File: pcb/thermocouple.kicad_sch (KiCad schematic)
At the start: 3 parts, among them J2 Conn_01x02, U4 MCP96RL00T-E_MX

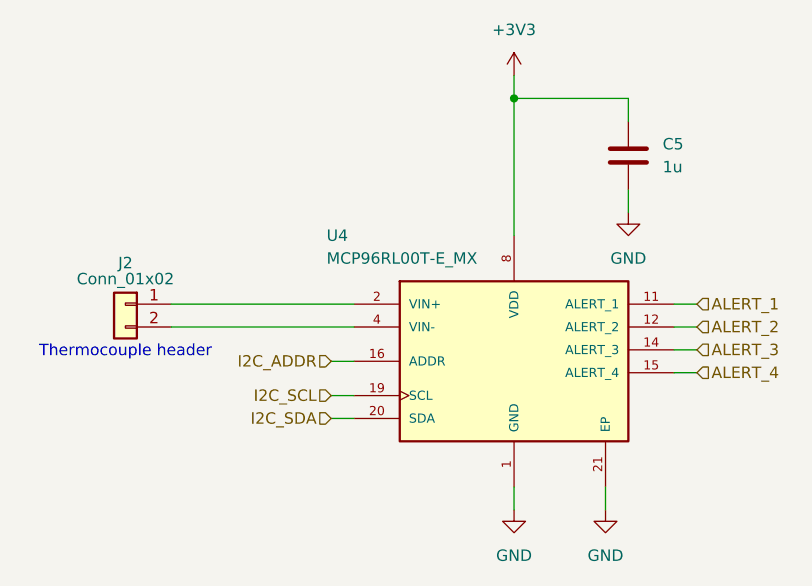
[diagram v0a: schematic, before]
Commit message: Update schematic for DE15
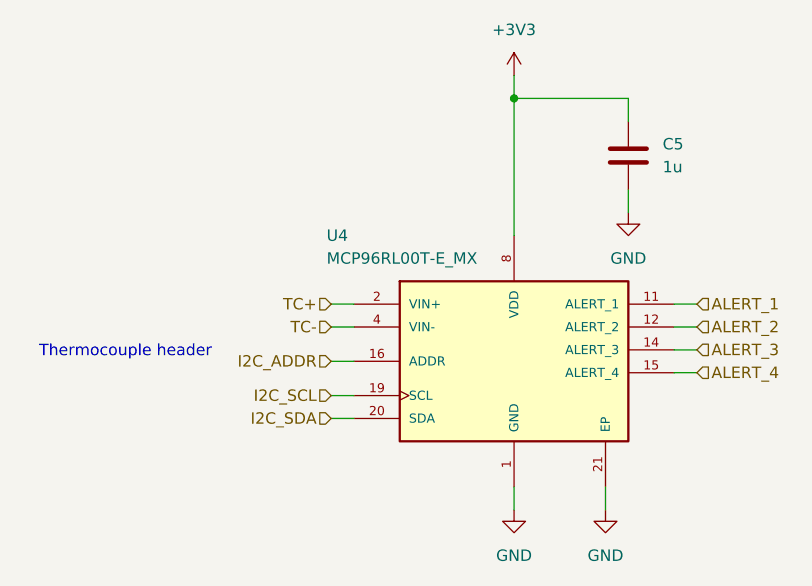
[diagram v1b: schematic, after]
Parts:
- removed J2: Conn_01x02, Connector_PinHeader_2.54mm:PinHeader_1x02_P2.54mm_Vertical, symbol Connector_Generic:Conn_01x02
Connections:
- net TC+: now reaches U4.2 (VIN+)
- net TC-: now reaches U4.4 (VIN-)
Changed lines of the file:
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@@
+	(wire
+		(pts
+			(xy 119.38 76.2) (xy 121.92 76.2)
+		)
+		(stroke
+			(width 0)
+			(type default)
+		)
+	)
+	(wire
+		(pts
+			(xy 119.38 78.74) (xy 121.92 78.74)
+		)
+		(stroke
+			(width 0)
+			(type default)
+		)
+	)
 	(wire
 		(pts
@@
 	(wire
 		(pts
-			(xy 101.6 78.74) (xy 121.92 78.74)
-		)
-		(stroke
-			(width 0)
-			(type default)
-		)
-	)
-	(wire
-		(pts
-			(xy 101.6 76.2) (xy 121.92 76.2)
-		)
-		(stroke
-			(width 0)
-			(type default)
-		)
-	)
-	(wire
-		(pts
 			(xy 119.38 86.36) (xy 121.92 86.36)
 		)
@@
 		)
 	)
+	(hierarchical_label "TC-"
+		(shape input)
+		(at 119.38 78.74 180)
+		(effects
+			(font
+				(size 1.27 1.27)
+			)
+			(justify right)
+		)
+	)
 	(hierarchical_label "ALERT_1"
 		(shape input)
@@
 			)
 			(justify left)
+		)
+	)
+	(hierarchical_label "TC+"
+		(shape input)
+		(at 119.38 76.2 180)
+		(effects
+			(font
+				(size 1.27 1.27)
+			)
+			(justify right)
 		)
 	)
@@
 					(unit 1)
 				)
-			)
-		)
-	)
-	(symbol
-		(lib_id "Connector_Generic:Conn_01x02")
-		(at 96.52 76.2 0)
-		(mirror y)
-		(unit 1)
-		(exclude_from_sim no)
-		(in_bom yes)
-		(on_board yes)
-		(dnp no)
-		(property "Reference" "J2"
-			(at 96.52 71.628 0)
-			(effects
-				(font
-					(size 1.27 1.27)
-				)
-			)
-		)
-		(property "Value" "Conn_01x02"
-			(at 96.52 73.406 0)
-			(effects
-				(font
-					(size 1.27 1.27)
-				)
-			)
-		)
-		(property "Footprint" "Connector_PinHeader_2.54mm:PinHeader_1x02_P2.54mm_Vertical"
-			(at 96.52 76.2 0)
-			(effects
-				(font
-					(size 1.27 1.27)
-				)
-				(hide yes)
-			)
-		)
-		(property "Datasheet" "~"
-			(at 96.52 76.2 0)
-			(effects
-				(font
-					(size 1.27 1.27)
-				)
-				(hide yes)
-			)
-		)
-		(property "Description" "Generic connector, single row, 01x02, script generated (kicad-library-utils/schlib/autogen/connector/)"
-			(at 96.52 76.2 0)
-			(effects
-				(font
-					(size 1.27 1.27)
-				)
-				(hide yes)
-			)
-		)
-		(pin "1"
-		)
-		(pin "2"
-		)
-		(instances
-			(project ""
-				(path "/c80bd5d9-8740-4998-9bee-52d12e7b4e76/78a70172-b7f8-4660-bb37-7ea5ee94a3dc"
-					(reference "J2")
-					(unit 1)
-				)
-				(path "/c80bd5d9-8740-4998-9bee-52d12e7b4e76/a8a83113-fc7e-4381-a556-8dc307a76abb"
-					(reference "J3")
-					(unit 1)
-				)
-				(path "/c80bd5d9-8740-4998-9bee-52d12e7b4e76/c2098876-5587-44d4-b0e7-9e452adf1def"
-					(reference "J5")
-					(unit 1)
-				)
-				(path "/c80bd5d9-8740-4998-9bee-52d12e7b4e76/dacb9b28-f0f9-4696-98b5-7e1301758de4"
-					(reference "J4")
-					(unit 1)
-				)

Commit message: Increase thermal vias to 0.3mm hole
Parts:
- U4: footprint Package_DFN_QFN:TQFN-20-1EP_5x5mm_P0.65mm_EP3.25x3.25mm_ThermalVias -> Package_DFN_QFN:TQFN-20-1EP_5x5mm_P0.65mm_EP3.25x3.25mm
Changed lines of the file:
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@@
 			)
 		)
-		(property "Footprint" "Package_DFN_QFN:TQFN-20-1EP_5x5mm_P0.65mm_EP3.25x3.25mm_ThermalVias"
+		(property "Footprint" "Package_DFN_QFN:TQFN-20-1EP_5x5mm_P0.65mm_EP3.25x3.25mm"
 			(at 139.7 86.36 0)
 			(effects

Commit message: Update production files
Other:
- note removed: "Thermocouple header"
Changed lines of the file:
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@@
 	(generator_version "9.0")
 	(paper "A4")
-	(text "Thermocouple header"
-		(exclude_from_sim no)
-		(at 96.52 81.534 0)
-		(effects
-			(font
-				(size 1.27 1.27)
-			)
-		)
-	)
 	(junction
 		(at 139.7 53.34)
